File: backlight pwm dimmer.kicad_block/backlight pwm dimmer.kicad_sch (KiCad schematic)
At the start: 3 parts, among them Q1 AO3400A

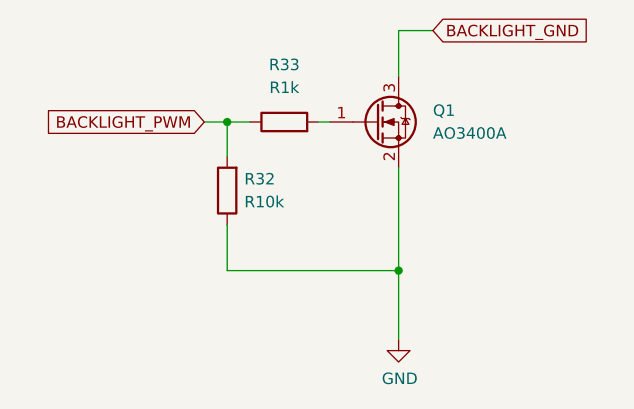
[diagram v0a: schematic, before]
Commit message: adjusted footprints for THT practicality
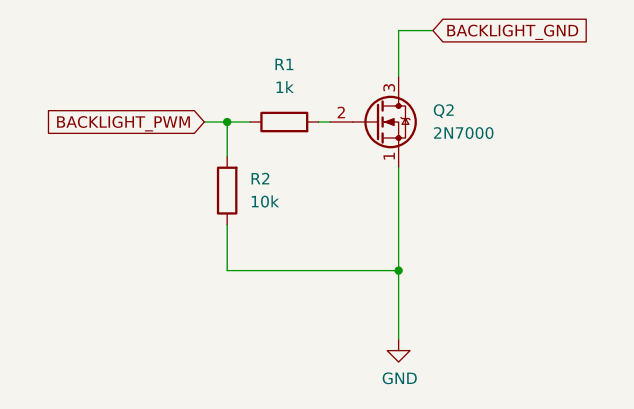
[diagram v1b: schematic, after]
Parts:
- removed Q1: AO3400A, Package_TO_SOT_SMD:SOT-23, symbol Transistor_FET:AO3400A
- added Q2: 2N7000, Package_TO_SOT_THT:TO-92L_Inline_Wide, symbol Transistor_FET:2N7000
- R1: renamed from R33; value R1k -> 1k; footprint Resistor_SMD:R_0603_1608Metric -> Resistor_THT:R_Axial_DIN0207_L6.3mm_D2.5mm_P10.16mm_Horizontal
- R2: renamed from R32; value R10k -> 10k; footprint Resistor_SMD:R_0603_1608Metric -> Resistor_THT:R_Axial_DIN0207_L6.3mm_D2.5mm_P10.16mm_Horizontal
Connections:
- net BACKLIGHT_GND: now also Q2.3 (D)
- net GND: now also Q2.1 (S)
- net at R1.2: now also Q2.2 (G)
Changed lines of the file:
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@@
+	)
+	(symbol
+		(lib_id "Transistor_FET:2N7000")
+		(at 252.73 142.24 0)
+		(unit 1)
+		(body_style 1)
+		(exclude_from_sim no)
+		(in_bom yes)
+		(on_board yes)
+		(in_pos_files yes)
+		(dnp no)
+		(fields_autoplaced yes)
+		(property "Reference" "Q2"
+			(at 259.08 140.9699 0)
+			(show_name no)
+			(do_not_autoplace no)
+			(effects
+				(font
+					(size 1.27 1.27)
+				)
+				(justify left)
+			)
+		)
+		(property "Value" "2N7000"
+			(at 259.08 143.5099 0)
+			(show_name no)
+			(do_not_autoplace no)
+			(effects
+				(font
+					(size 1.27 1.27)
+				)
+				(justify left)
+			)
+		)
+		(property "Footprint" "Package_TO_SOT_THT:TO-92L_Inline_Wide"
+			(at 257.81 144.145 0)
+			(hide yes)
+			(show_name no)
+			(do_not_autoplace no)
+			(effects
+				(font
+					(size 1.27 1.27)
+					(italic yes)
+				)
+				(justify left)
+			)
+		)
+		(property "Datasheet" "https://www.vishay.com/docs/70226/70226.pdf"
+			(at 257.81 146.05 0)
+			(hide yes)
+			(show_name no)
+			(do_not_autoplace no)
+			(effects
+				(font
+					(size 1.27 1.27)
+				)
+				(justify left)
+			)
+		)
+		(property "Description" "0.2A Id, 200V Vds, N-Channel MOSFET, 2.6V Logic Level, TO-92"
+			(at 252.73 142.24 0)
+			(hide yes)
+			(show_name no)
+			(do_not_autoplace no)
+			(effects
+				(font
+					(size 1.27 1.27)
+				)
+			)
+		)
+		(pin "1"
+		)
+		(pin "2"
+		)
+		(pin "3"
+		)
+		(instances
+			(project "kicad-mobiflight-device-blocks-worksheet"
+				(path "/4714e232-3dfb-45f4-a0c3-3539b78f5138"
+					(reference "Q2")
+					(unit 1)
+				)
+			)
+		)
 	)
 	(symbol
@@
 		(dnp no)
 		(fields_autoplaced yes)
-		(property "Reference" "R32"
-			(at 238.125 148.59 0)
+		(property "Reference" "R2"
+			(at 238.76 148.5899 0)
 			(show_name no)
 			(do_not_autoplace no)
@@
 			)
 		)
-		(property "Value" "R10k"
-			(at 238.125 151.13 0)
+		(property "Value" "10k"
+			(at 238.76 151.1299 0)
 			(show_name no)
 			(do_not_autoplace no)
@@
 			)
 		)
-		(property "Footprint" "Resistor_SMD:R_0603_1608Metric"
+		(property "Footprint" "Resistor_THT:R_Axial_DIN0207_L6.3mm_D2.5mm_P10.16mm_Horizontal"
 			(at 237.998 149.86 90)
 			(hide yes)
@@
 			(project "kicad-mobiflight-device-blocks-worksheet"
 				(path "/4714e232-3dfb-45f4-a0c3-3539b78f5138"
-					(reference "R32")
+					(reference "R2")
 					(unit 1)
 				)
@@
 	)
 	(symbol
-		(lib_id "Transistor_FET:AO3400A")
-		(at 252.73 142.24 0)
-		(unit 1)
-		(body_style 1)
-		(exclude_from_sim no)
-		(in_bom yes)
-		(on_board yes)
-		(in_pos_files yes)
-		(dnp no)
-		(fields_autoplaced yes)
-		(property "Reference" "Q1"
-			(at 259.08 140.97 0)
-			(show_name no)
-			(do_not_autoplace no)
-			(effects
-				(font
-					(size 1.27 1.27)
-				)
-				(justify left)
-			)
-		)
-		(property "Value" "AO3400A"
-			(at 259.08 143.51 0)
-			(show_name no)
-			(do_not_autoplace no)
-			(effects
-				(font
-					(size 1.27 1.27)
-				)
-				(justify left)
-			)
-		)
-		(property "Footprint" "Package_TO_SOT_SMD:SOT-23"
-			(at 257.81 144.145 0)
-			(hide yes)
-			(show_name no)
-			(do_not_autoplace no)
-			(effects
-				(font
-					(size 1.27 1.27)
-					(italic yes)
-				)
-				(justify left)
-			)
-		)
-		(property "Datasheet" "http://www.aosmd.com/pdfs/datasheet/AO3400A.pdf"
-			(at 252.73 142.24 0)
-			(hide yes)
-			(show_name no)
-			(do_not_autoplace no)
-			(effects
-				(font
-					(size 1.27 1.27)
-				)
-				(justify left)
-			)
-		)
-		(property "Description" ""
-			(at 252.73 142.24 0)
-			(hide yes)
-			(show_name no)
-			(do_not_autoplace no)
-			(effects
-				(font
-					(size 1.27 1.27)
-				)
-			)
-		)
-		(property "LCSC Part #" " C20917"
-			(at 252.73 142.24 0)
-			(hide yes)
-			(show_name no)
-			(do_not_autoplace no)
-			(effects
-				(font
-					(size 1.27 1.27)
-				)
-			)
-		)
-		(pin "1"
-		)
-		(pin "2"
-		)
-		(pin "3"
-		)
-		(instances
-			(project "kicad-mobiflight-device-blocks-worksheet"
-				(path "/4714e232-3dfb-45f4-a0c3-3539b78f5138"
-					(reference "Q1")
-					(unit 1)
-				)
-			)
-		)
-	)
-	(symbol
 		(lib_id "Device:R")
 		(at 242.57 142.24 90)
@@
 		(dnp no)
 		(fields_autoplaced yes)
-		(property "Reference" "R33"
+		(property "Reference" "R1"
 			(at 242.57 135.89 90)
 			(show_name no)
@@
 			)
 		)
-		(property "Value" "R1k"
+		(property "Value" "1k"
 			(at 242.57 138.43 90)
 			(show_name no)
@@
 			)
 		)
-		(property "Footprint" "Resistor_SMD:R_0603_1608Metric"
+		(property "Footprint" "Resistor_THT:R_Axial_DIN0207_L6.3mm_D2.5mm_P10.16mm_Horizontal"
 			(at 242.57 144.018 90)
 			(hide yes)
@@
 			(project "kicad-mobiflight-device-blocks-worksheet"
 				(path "/4714e232-3dfb-45f4-a0c3-3539b78f5138"
-					(reference "R33")
+					(reference "R1")
 					(unit 1)
 				)
